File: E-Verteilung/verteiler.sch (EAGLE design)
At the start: 38 parts, among them K1.3 ESB63-40-230AC/DC, K1.7 RELAIS_2-POL-UM, P1.25 E219-3, Q1.13 FEHLER-STROM-SCHUTZSCHALTER_4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, Q1.17 FEHLER-STROM-SCHUTZSCHALTER_4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, Q1.21 FEHLER-STROM-SCHUTZSCHALTER_4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, Q1.25 E203-40, Q1.28 F202A-40

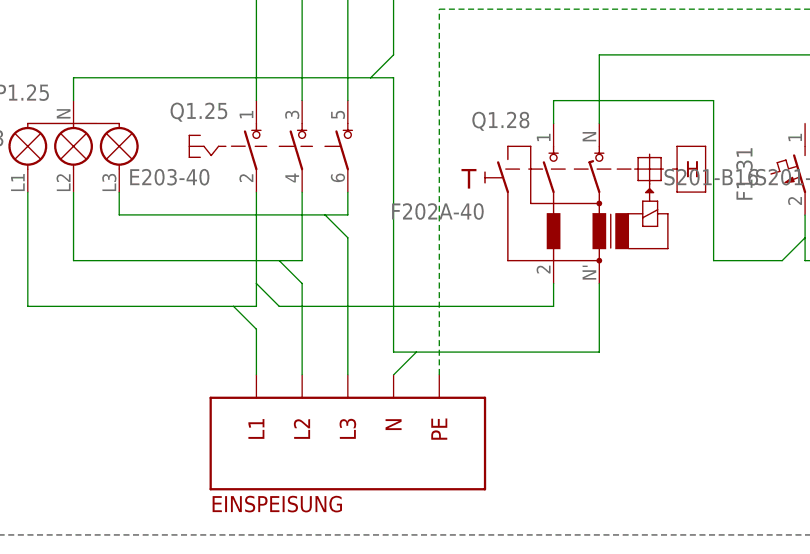
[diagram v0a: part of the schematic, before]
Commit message: Changed IT from phase L1 to L3
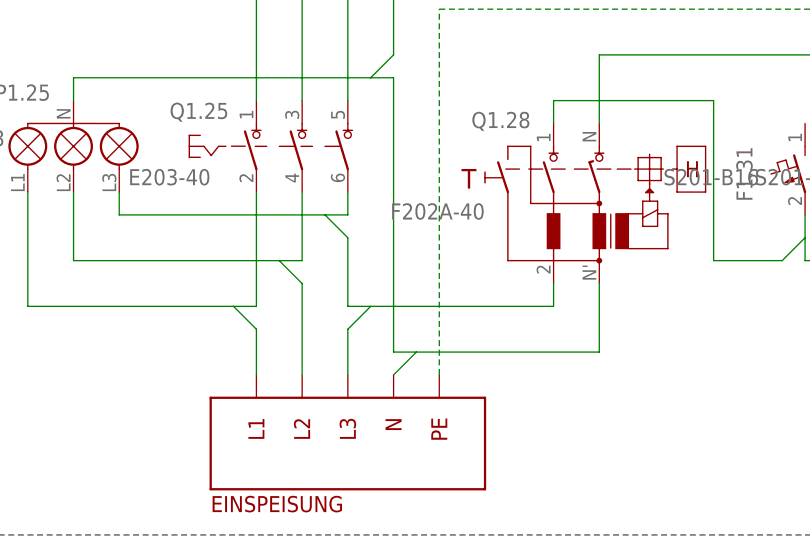
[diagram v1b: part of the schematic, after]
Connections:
- new net N$7: P1.25.L3, Q1.25.6
- net L1-EXT: no longer Q1.28.2
- net L3-EXT: now also Q1.28.2; no longer P1.25.L3, Q1.25.6
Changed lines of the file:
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@@
 <wire x1="12.7" y1="27.94" x2="12.7" y2="40.64" width="0.1524" layer="91"/>
 <pinref part="Q1.25" gate="G$1" pin="2"/>
-<wire x1="38.1" y1="30.48" x2="38.1" y2="40.64" width="0.1524" layer="91"/>
-<pinref part="Q1.28" gate="G$1" pin="2"/>
-<wire x1="71.12" y1="27.94" x2="71.12" y2="30.48" width="0.1524" layer="91"/>
-<wire x1="71.12" y1="27.94" x2="40.64" y2="27.94" width="0.1524" layer="91"/>
-<wire x1="40.64" y1="27.94" x2="38.1" y2="30.48" width="0.1524" layer="91"/>
+<wire x1="38.1" y1="27.94" x2="38.1" y2="40.64" width="0.1524" layer="91"/>
 <wire x1="35.56" y1="27.94" x2="38.1" y2="27.94" width="0.1524" layer="91"/>
-<wire x1="38.1" y1="30.48" x2="38.1" y2="27.94" width="0.1524" layer="91"/>
-</segment>
-</net>
-<net name="L3-EXT" class="0">
-<segment>
-<pinref part="ESP1" gate="G$1" pin="L3-EXT"/>
-<pinref part="Q1.25" gate="G$1" pin="6"/>
-<wire x1="48.26" y1="20.32" x2="48.26" y2="35.56" width="0.1524" layer="91"/>
-<wire x1="48.26" y1="38.1" x2="48.26" y2="40.64" width="0.1524" layer="91"/>
-<wire x1="48.26" y1="35.56" x2="45.72" y2="38.1" width="0.1524" layer="91"/>
-<wire x1="45.72" y1="38.1" x2="22.86" y2="38.1" width="0.1524" layer="91"/>
-<wire x1="22.86" y1="38.1" x2="22.86" y2="40.64" width="0.1524" layer="91"/>
-<pinref part="P1.25" gate="G$1" pin="L3"/>
-<wire x1="45.72" y1="38.1" x2="48.26" y2="38.1" width="0.1524" layer="91"/>
 </segment>
 </net>
@@
 </segment>
 </net>
+<net name="N$7" class="0">
+<segment>
+<pinref part="Q1.25" gate="G$1" pin="6"/>
+<wire x1="48.26" y1="38.1" x2="48.26" y2="40.64" width="0.1524" layer="91"/>
+<wire x1="48.26" y1="35.56" x2="45.72" y2="38.1" width="0.1524" layer="91"/>
+<wire x1="45.72" y1="38.1" x2="22.86" y2="38.1" width="0.1524" layer="91"/>
+<wire x1="22.86" y1="38.1" x2="22.86" y2="40.64" width="0.1524" layer="91"/>
+<pinref part="P1.25" gate="G$1" pin="L3"/>
+<wire x1="45.72" y1="38.1" x2="48.26" y2="38.1" width="0.1524" layer="91"/>
+<wire x1="48.26" y1="35.56" x2="48.26" y2="27.94" width="0.1524" layer="91"/>
+</segment>
+</net>
+<net name="L3-EXT" class="0">
+<segment>
+<pinref part="Q1.28" gate="G$1" pin="2"/>
+<wire x1="71.12" y1="27.94" x2="71.12" y2="30.48" width="0.1524" layer="91"/>
+<wire x1="71.12" y1="27.94" x2="50.8" y2="27.94" width="0.1524" layer="91"/>
+<wire x1="50.8" y1="27.94" x2="48.26" y2="25.4" width="0.1524" layer="91"/>
+<pinref part="ESP1" gate="G$1" pin="L3-EXT"/>
+<wire x1="48.26" y1="25.4" x2="48.26" y2="20.32" width="0.1524" layer="91"/>
+<wire x1="48.26" y1="27.94" x2="50.8" y2="27.94" width="0.1524" layer="91"/>
+</segment>
+</net>

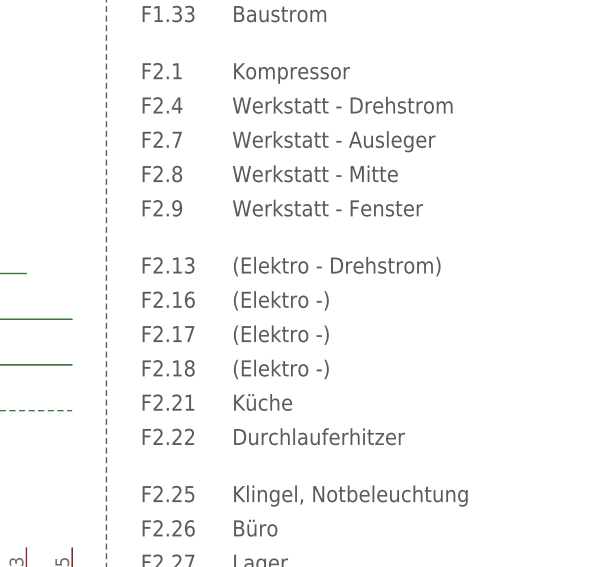
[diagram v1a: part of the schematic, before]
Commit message: Updates for kitchen area
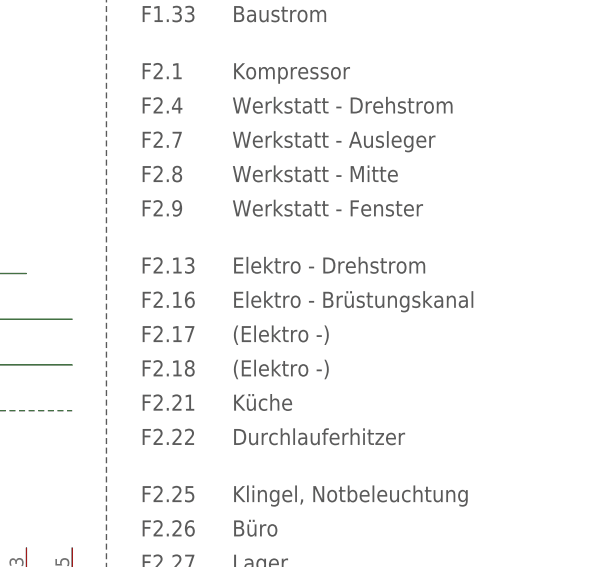
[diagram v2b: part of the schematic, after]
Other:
- note added: "Elektro - Brüstungskanal"
- note added: "Elektro - Drehstrom"
- note removed: "(Elektro - Drehstrom)"
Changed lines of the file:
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@@
 <text x="251.46" y="142.24" size="1.778" layer="97">Werkstatt - Mitte</text>
 <text x="251.46" y="138.43" size="1.778" layer="97">Werkstatt - Fenster</text>
-<text x="251.46" y="132.08" size="1.778" layer="97">(Elektro - Drehstrom)</text>
-<text x="251.46" y="128.27" size="1.778" layer="97">(Elektro -)</text>
+<text x="251.46" y="132.08" size="1.778" layer="97">Elektro - Drehstrom</text>
+<text x="251.46" y="128.27" size="1.778" layer="97">Elektro - Brüstungskanal</text>
 <text x="251.46" y="120.65" size="1.778" layer="97">(Elektro -)</text>
 <text x="251.46" y="124.46" size="1.778" layer="97">(Elektro -)</text>

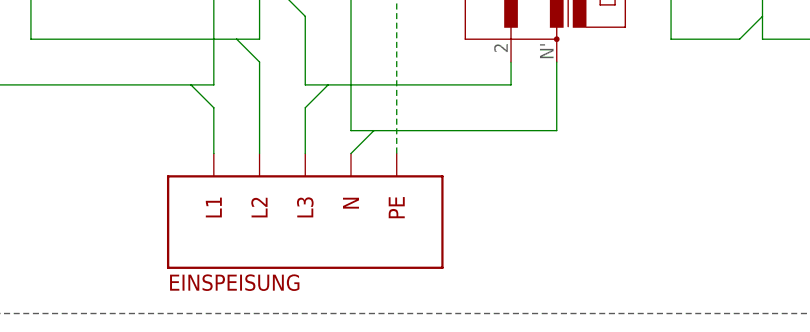
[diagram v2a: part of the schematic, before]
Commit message: Added supply name
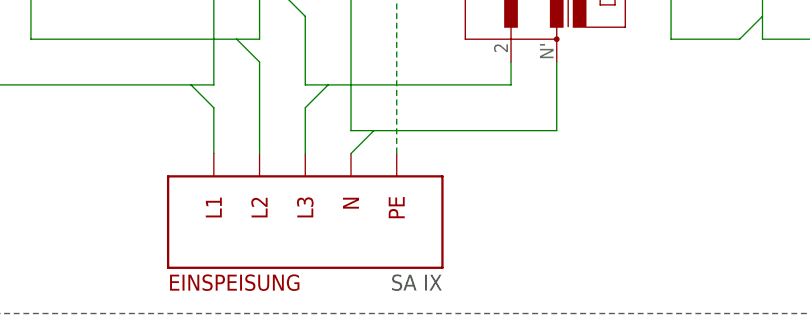
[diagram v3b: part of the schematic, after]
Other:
- note added: "SA IX"
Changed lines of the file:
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@@
 <text x="251.46" y="116.84" size="1.778" layer="97">Küche</text>
 <text x="251.46" y="113.03" size="1.778" layer="97">Durchlauferhitzer</text>
+<text x="63.5" y="5.08" size="1.778" layer="97" align="bottom-right">SA IX</text>
 </plain>
 <instances>
